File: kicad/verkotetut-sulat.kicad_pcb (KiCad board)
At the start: 2 copper layers, 73.7 x 55.9 mm, 19 parts, among them P101 GPIO and ADC, P102 Programming pins, P103 Battery connection, P104 USB2Serial_connection, SW101 SW_PUSH, SW102 SPST, U101 ESP-12E, U102 LM317T

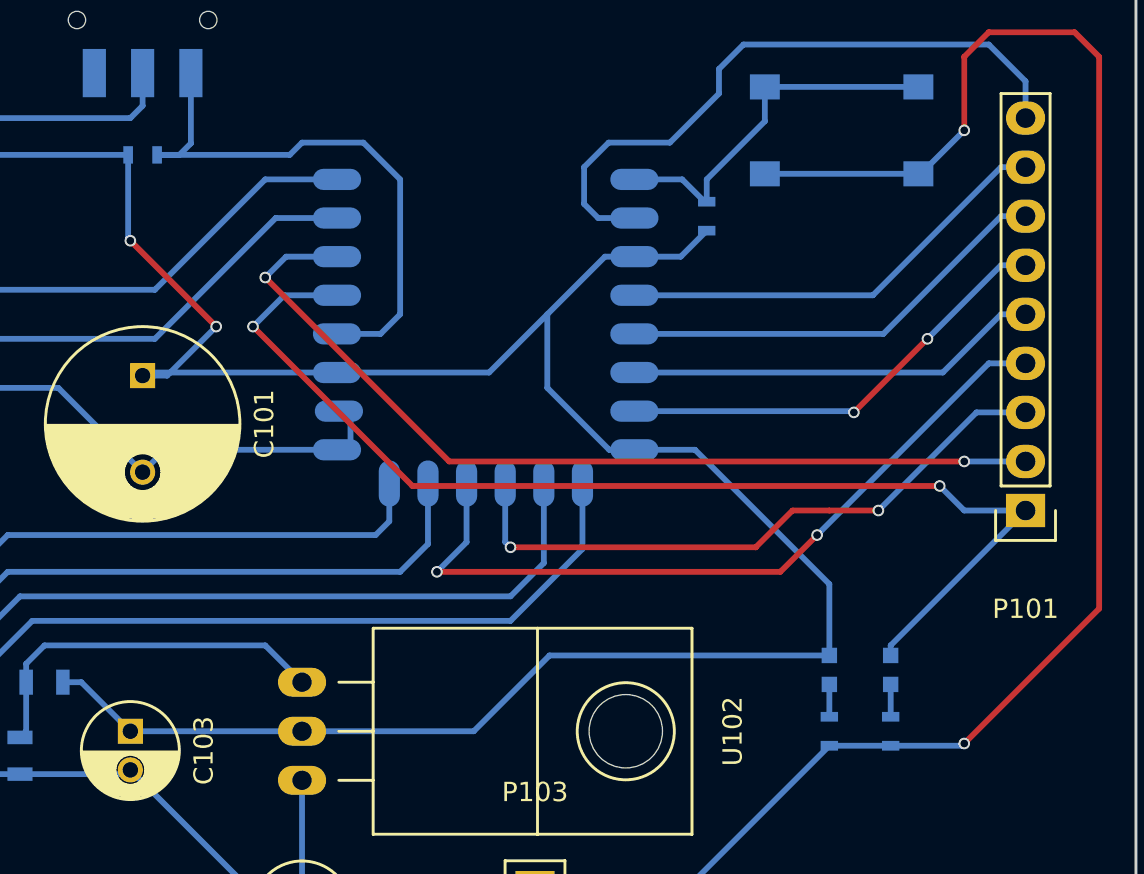
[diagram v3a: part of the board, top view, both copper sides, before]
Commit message: Increase via size
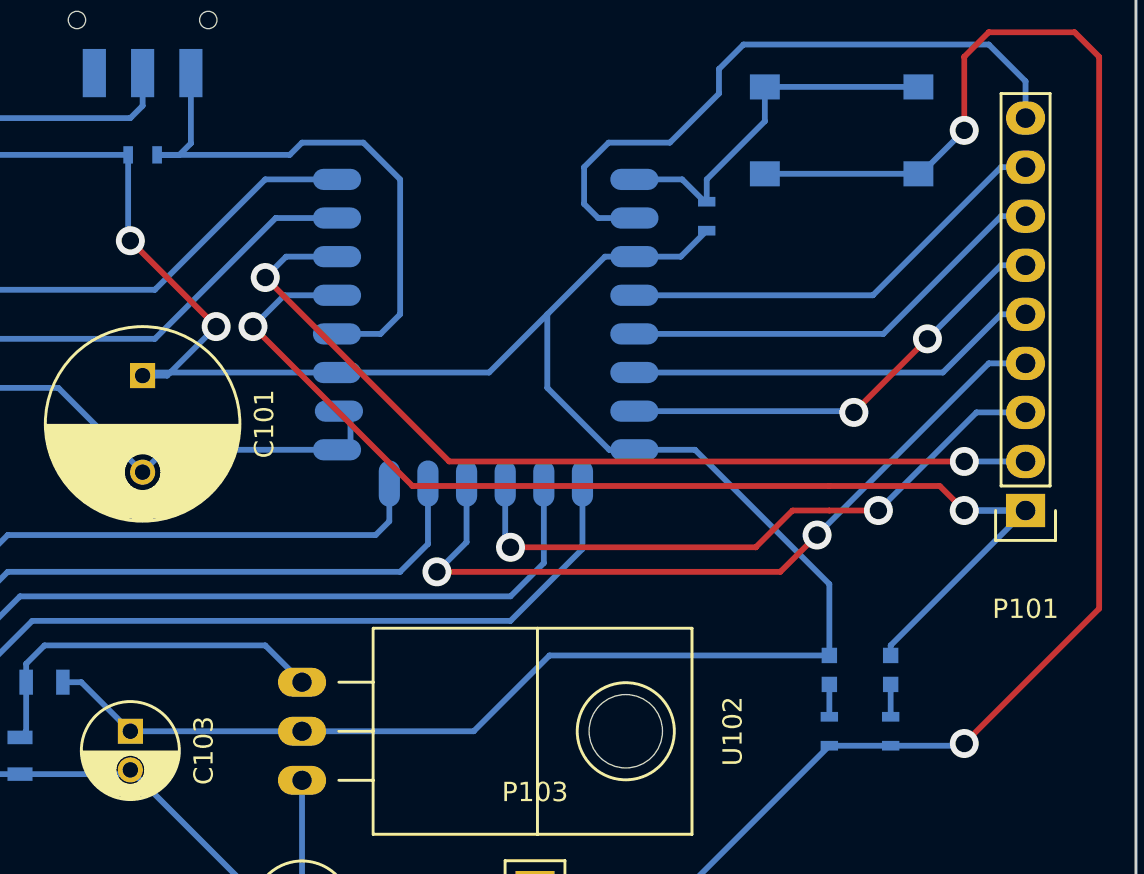
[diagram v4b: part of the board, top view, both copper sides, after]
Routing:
- net GPIO4: track 60.1 -> 63.2 mm
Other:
- net class Default: via_dia 0.6 -> 1.5; via_drill 0.4 -> 0.9
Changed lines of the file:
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@@
     (links 49)
     (no_connects 0)
-    (area 109.214761 62.315 186.130001 126.440001)
+    (area 112.319999 70.409999 186.130001 126.440001)
     (thickness 1.6)
     (drawings 4)
-    (tracks 183)
+    (tracks 185)
     (zones 0)
     (modules 19)
@@
     (segment_width 0.2)
     (edge_width 0.15)
-    (via_size 0.6)
-    (via_drill 0.4)
+    (via_size 1.5)
+    (via_drill 0.9)
     (via_min_size 0.4)
     (via_min_drill 0.3)
@@
     (clearance 0.3)
     (trace_width 0.3)
-    (via_dia 0.6)
-    (via_drill 0.4)
+    (via_dia 1.5)
+    (via_drill 0.9)
     (uvia_dia 0.3)
     (uvia_drill 0.1)
@@
   (segment (start 135.89 90.805) (end 134.62 90.805) (width 0.3) (layer B.Cu) (net 1))
   (segment (start 138.43 88.265) (end 135.89 90.805) (width 0.3) (layer B.Cu) (net 1))
-  (via (at 138.43 88.265) (size 0.6) (drill 0.4) (layers F.Cu B.Cu) (net 1))
+  (via (at 138.43 88.265) (size 1.5) (drill 0.9) (layers F.Cu B.Cu) (net 1))
   (segment (start 133.985 83.82) (end 138.43 88.265) (width 0.3) (layer F.Cu) (net 1))
-  (via (at 133.985 83.82) (size 0.6) (drill 0.4) (layers F.Cu B.Cu) (net 1))
+  (via (at 133.985 83.82) (size 1.5) (drill 0.9) (layers F.Cu B.Cu) (net 1))
   (segment (start 133.87 83.705) (end 133.985 83.82) (width 0.3) (layer B.Cu) (net 1))
   (segment (start 142.875 109.22) (end 151.765 109.22) (width 0.3) (layer B.Cu) (net 1))
@@
   (segment (start 177.05 109.97) (end 173.355 109.97) (width 0.3) (layer B.Cu) (net 2))
   (segment (start 177.165 109.855) (end 177.05 109.97) (width 0.3) (layer B.Cu) (net 2))
-  (via (at 177.165 109.855) (size 0.6) (drill 0.4) (layers F.Cu B.Cu) (net 2))
+  (via (at 177.165 109.855) (size 1.5) (drill 0.9) (layers F.Cu B.Cu) (net 2))
   (segment (start 184.15 102.87) (end 177.165 109.855) (width 0.3) (layer F.Cu) (net 2))
   (segment (start 184.15 74.295) (end 184.15 102.87) (width 0.3) (layer F.Cu) (net 2))
@@
   (segment (start 177.165 74.295) (end 178.435 73.025) (width 0.3) (layer F.Cu) (net 2))
   (segment (start 177.165 78.105) (end 177.165 74.295) (width 0.3) (layer F.Cu) (net 2))
-  (via (at 177.165 78.105) (size 0.6) (drill 0.4) (layers F.Cu B.Cu) (net 2))
+  (via (at 177.165 78.105) (size 1.5) (drill 0.9) (layers F.Cu B.Cu) (net 2))
   (segment (start 170.18 109.97) (end 173.355 109.97) (width 0.3) (layer B.Cu) (net 2))
   (segment (start 118.11 91.44) (end 130.255 91.44) (width 0.3) (layer B.Cu) (net 2))
@@
   (segment (start 142.875 111.76) (end 142.875 117.475) (width 0.3) (layer B.Cu) (net 3))
   (segment (start 154.94 117.475) (end 142.875 117.475) (width 0.3) (layer B.Cu) (net 3))
+  (segment (start 170.18 96.52) (end 175.895 96.52) (width 0.3) (layer F.Cu) (net 4))
+  (segment (start 175.895 96.52) (end 177.165 97.79) (width 0.3) (layer F.Cu) (net 4))
+  (via (at 177.165 97.79) (size 1.5) (drill 0.9) (layers F.Cu B.Cu) (net 4))
+  (segment (start 177.165 97.79) (end 180.34 97.79) (width 0.3) (layer B.Cu) (net 4))
   (segment (start 145.385 86.645) (end 141.955 86.645) (width 0.3) (layer B.Cu) (net 4))
   (segment (start 177.165 97.79) (end 180.34 97.79) (width 0.3) (layer B.Cu) (net 4))
-  (segment (start 175.895 96.52) (end 177.165 97.79) (width 0.3) (layer B.Cu) (net 4))
-  (via (at 175.895 96.52) (size 0.6) (drill 0.4) (layers F.Cu B.Cu) (net 4))
-  (segment (start 148.59 96.52) (end 175.895 96.52) (width 0.3) (layer F.Cu) (net 4))
+  (segment (start 148.59 96.52) (end 170.18 96.52) (width 0.3) (layer F.Cu) (net 4))
   (segment (start 140.335 88.265) (end 148.59 96.52) (width 0.3) (layer F.Cu) (net 4))
-  (via (at 140.335 88.265) (size 0.6) (drill 0.4) (layers F.Cu B.Cu) (net 4))
+  (via (at 140.335 88.265) (size 1.5) (drill 0.9) (layers F.Cu B.Cu) (net 4))
   (segment (start 141.955 86.645) (end 140.335 88.265) (width 0.3) (layer B.Cu) (net 4))
   (segment (start 173.355 105.2957) (end 173.355 104.775) (width 0.3) (layer B.Cu) (net 4))
@@
   (segment (start 145.385 84.645) (end 142.05 84.645) (width 0.3) (layer B.Cu) (net 7))
   (segment (start 177.165 95.25) (end 180.34 95.25) (width 0.3) (layer B.Cu) (net 7))
-  (via (at 177.165 95.25) (size 0.6) (drill 0.4) (layers F.Cu B.Cu) (net 7))
+  (via (at 177.165 95.25) (size 1.5) (drill 0.9) (layers F.Cu B.Cu) (net 7))
   (segment (start 150.495 95.25) (end 177.165 95.25) (width 0.3) (layer F.Cu) (net 7))
   (segment (start 140.97 85.725) (end 150.495 95.25) (width 0.3) (layer F.Cu) (net 7))
-  (via (at 140.97 85.725) (size 0.6) (drill 0.4) (layers F.Cu B.Cu) (net 7))
+  (via (at 140.97 85.725) (size 1.5) (drill 0.9) (layers F.Cu B.Cu) (net 7))
   (segment (start 142.05 84.645) (end 140.97 85.725) (width 0.3) (layer B.Cu) (net 7))
   (segment (start 170.18 97.79) (end 172.72 97.79) (width 0.3) (layer F.Cu) (net 8))
-  (via (at 172.72 97.79) (size 0.6) (drill 0.4) (layers F.Cu B.Cu) (net 8))
+  (via (at 172.72 97.79) (size 1.5) (drill 0.9) (layers F.Cu B.Cu) (net 8))
   (segment (start 153.395 96.395) (end 153.395 99.42) (width 0.3) (layer B.Cu) (net 8))
   (segment (start 177.8 92.71) (end 180.34 92.71) (width 0.3) (layer B.Cu) (net 8))
@@
   (segment (start 166.37 99.695) (end 168.275 97.79) (width 0.3) (layer F.Cu) (net 8))
   (segment (start 153.67 99.695) (end 166.37 99.695) (width 0.3) (layer F.Cu) (net 8))
-  (via (at 153.67 99.695) (size 0.6) (drill 0.4) (layers F.Cu B.Cu) (net 8))
+  (via (at 153.67 99.695) (size 1.5) (drill 0.9) (layers F.Cu B.Cu) (net 8))
   (segment (start 153.395 99.42) (end 153.67 99.695) (width 0.3) (layer B.Cu) (net 8))
   (segment (start 180.34 90.17) (end 178.435 90.17) (width 0.3) (layer B.Cu) (net 9))
   (segment (start 151.395 99.43) (end 151.395 96.395) (width 0.3) (layer B.Cu) (net 9))
   (segment (start 149.86 100.965) (end 151.395 99.43) (width 0.3) (layer B.Cu) (net 9))
-  (via (at 149.86 100.965) (size 0.6) (drill 0.4) (layers F.Cu B.Cu) (net 9))
+  (via (at 149.86 100.965) (size 1.5) (drill 0.9) (layers F.Cu B.Cu) (net 9))
   (segment (start 167.64 100.965) (end 149.86 100.965) (width 0.3) (layer F.Cu) (net 9))
   (segment (start 169.545 99.06) (end 167.64 100.965) (width 0.3) (layer F.Cu) (net 9))
-  (via (at 169.545 99.06) (size 0.6) (drill 0.4) (layers F.Cu B.Cu) (net 9))
+  (via (at 169.545 99.06) (size 1.5) (drill 0.9) (layers F.Cu B.Cu) (net 9))
   (segment (start 178.435 90.17) (end 169.545 99.06) (width 0.3) (layer B.Cu) (net 9))
   (segment (start 159.385 90.645) (end 176.055 90.645) (width 0.3) (layer B.Cu) (net 10))
@@
   (segment (start 171.385 92.645) (end 159.385 92.645) (width 0.3) (layer B.Cu) (net 11))
   (segment (start 171.45 92.71) (end 171.385 92.645) (width 0.3) (layer B.Cu) (net 11))
-  (via (at 171.45 92.71) (size 0.6) (drill 0.4) (layers F.Cu B.Cu) (net 11))
+  (via (at 171.45 92.71) (size 1.5) (drill 0.9) (layers F.Cu B.Cu) (net 11))
   (segment (start 175.26 88.9) (end 171.45 92.71) (width 0.3) (layer F.Cu) (net 11))
-  (via (at 175.26 88.9) (size 0.6) (drill 0.4) (layers F.Cu B.Cu) (net 11))
+  (via (at 175.26 88.9) (size 1.5) (drill 0.9) (layers F.Cu B.Cu) (net 11))
   (segment (start 179.07 85.09) (end 175.26 88.9) (width 0.3) (layer B.Cu) (net 11))
   (segment (start 159.385 88.645) (end 172.975 88.645) (width 0.3) (layer B.Cu) (net 12))

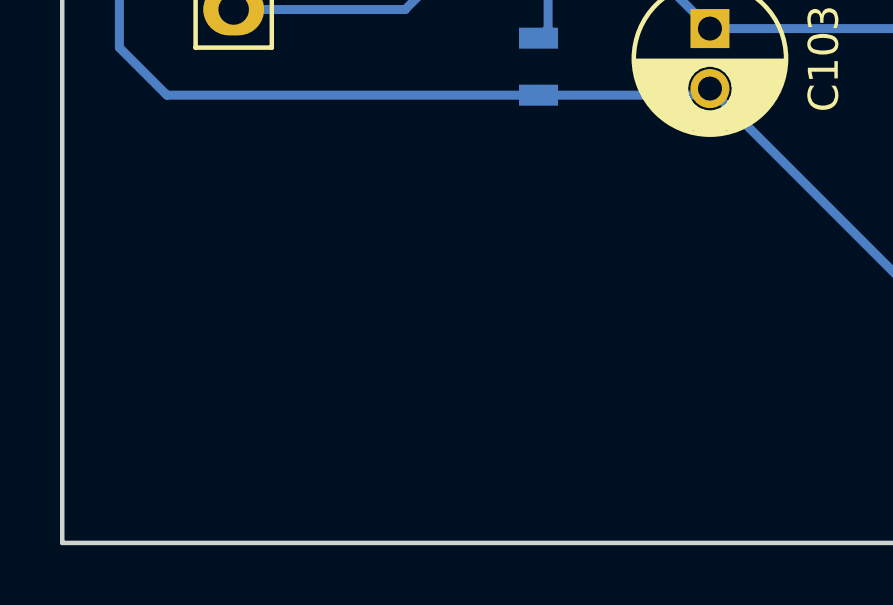
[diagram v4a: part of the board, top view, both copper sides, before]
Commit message: Add text to board
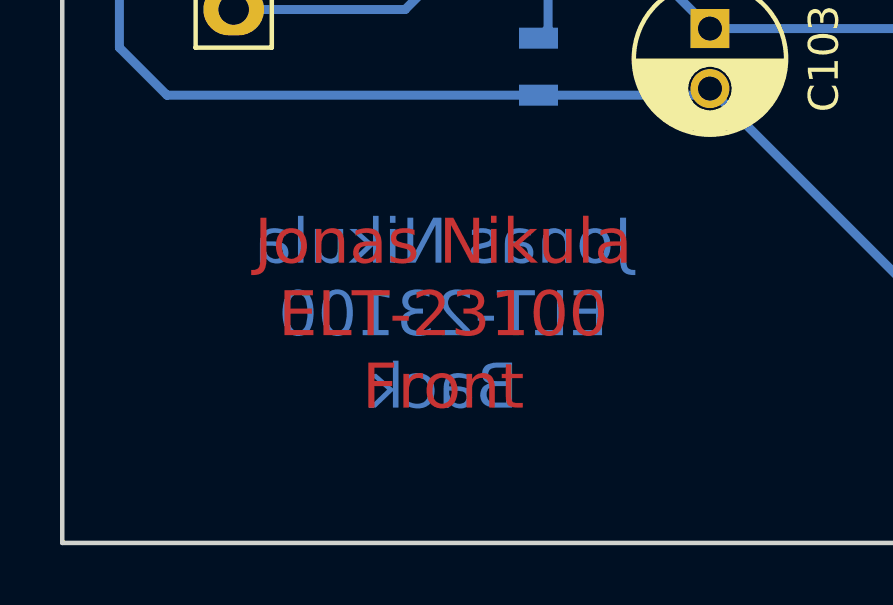
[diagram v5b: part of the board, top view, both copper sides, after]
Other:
- board text added: "Jonas Nikula ELT-23100 Back"
- board text added: "Jonas Nikula ELT-23100 Front"
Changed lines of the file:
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@@
     (area 112.319999 70.409999 186.130001 126.440001)
     (thickness 1.6)
-    (drawings 4)
+    (drawings 6)
     (tracks 185)
     (zones 0)
@@
       (outputformat 1)
       (mirror false)
-      (drillshape 1)
+      (drillshape 0)
       (scaleselection 1)
       (outputdirectory ""))
@@
     )
   )
+  (gr_text "Jonas Nikula\nELT-23100\nFront" (at 125.095 118.745) (layer F.Cu)
+    (effects (font (size 1.5 1.5) (thickness 0.3)))
+  )
+  (gr_text "Jonas Nikula\nELT-23100\nBack" (at 125.095 118.745) (layer B.Cu)
+    (effects (font (size 1.5 1.5) (thickness 0.3)) (justify mirror))
+  )
   (gr_line (start 112.395 126.365) (end 112.395 70.485) (angle 90) (layer Edge.Cuts) (width 0.15))
